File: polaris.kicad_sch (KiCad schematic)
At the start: 19 parts, among them J101 XT60-M, J102 PYRO0, J103 PYRO1, J104 PYRO2, J105 PYRO3, J106 PYRO4, J107 PYRO5, J108 FIN1, J109 FIN2, J110 FIN3, J111 FIN4

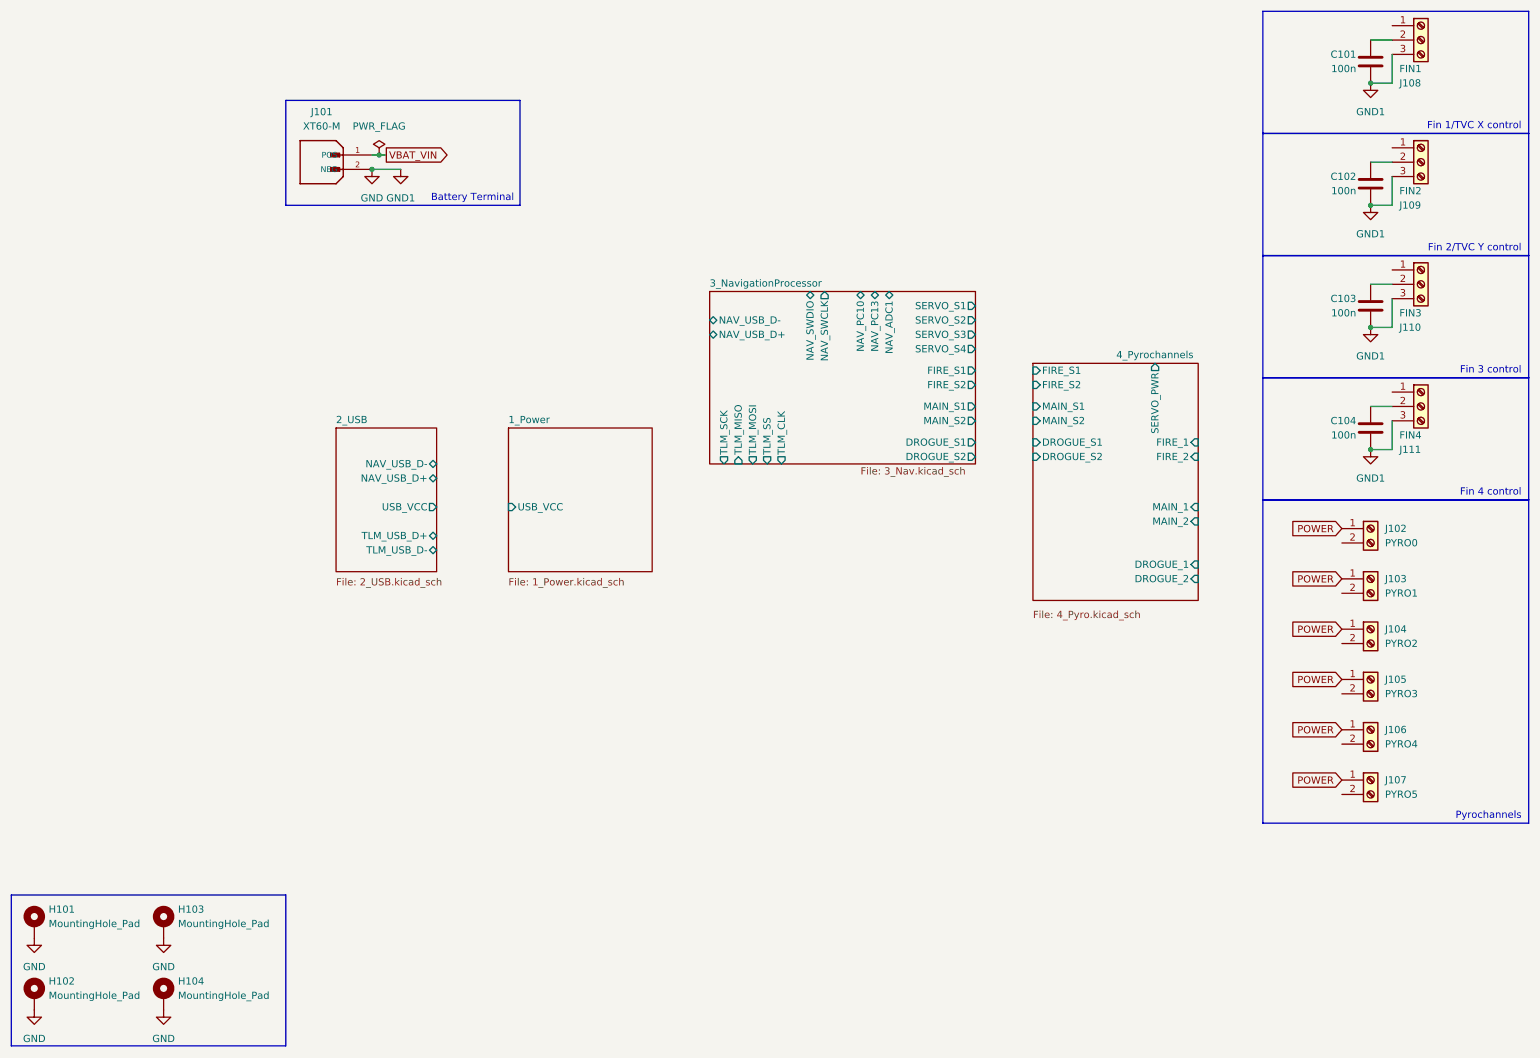
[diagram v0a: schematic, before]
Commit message: Finished restructuring schematic
Most components that were on page 3 are now in their own page
Added high-frequency 4.7 uF capacitor to servo power line
Continuity sensing on pyrochannels is multiplexed to one ADC on NAV.
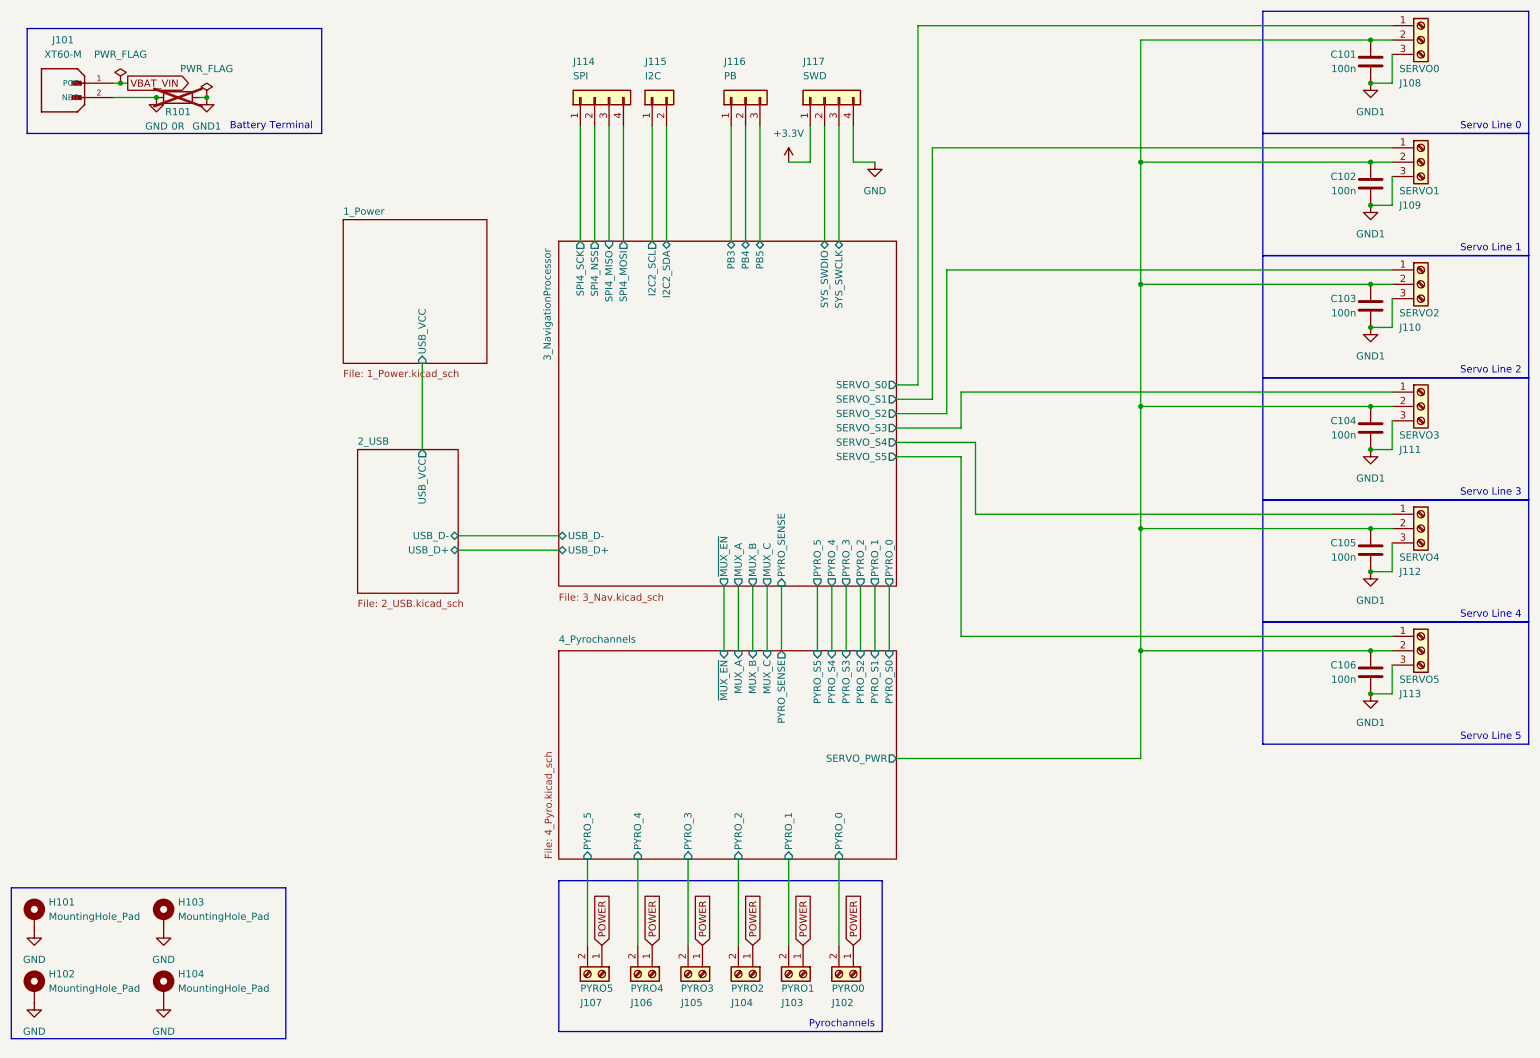
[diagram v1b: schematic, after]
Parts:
- added C105, C106: 100n, Capacitor_SMD:C_0603_1608Metric, symbol Device:C
- added J112: SERVO4, TerminalBlock:TerminalBlock_Xinya_XY308-2.54-3P_1x03_P2.54mm_Horizontal, symbol Connector:Screw_Terminal_01x03
- added J113: SERVO5, TerminalBlock:TerminalBlock_Xinya_XY308-2.54-3P_1x03_P2.54mm_Horizontal, symbol Connector:Screw_Terminal_01x03
- added J114: SPI, TerminalBlock:TerminalBlock_Xinya_XY308-2.54-4P_1x04_P2.54mm_Horizontal, symbol Connector_Generic:Conn_01x04
- added J115: I2C, TerminalBlock:TerminalBlock_Xinya_XY308-2.54-2P_1x02_P2.54mm_Horizontal, symbol Connector_Generic:Conn_01x02
- added J116: PB, TerminalBlock:TerminalBlock_Xinya_XY308-2.54-3P_1x03_P2.54mm_Horizontal, symbol Connector_Generic:Conn_01x03
- added J117: SWD, TerminalBlock:TerminalBlock_Xinya_XY308-2.54-4P_1x04_P2.54mm_Horizontal, symbol Connector_Generic:Conn_01x04
- added R101: 0R, Resistor_SMD:R_0603_1608Metric, symbol Device:R
- J108: value FIN1 -> SERVO0
- J109: value FIN2 -> SERVO1
- J110: value FIN3 -> SERVO2
- J111: value FIN4 -> SERVO3
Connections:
- net 3_NavigationProcessor/SERVO_S1: now also J109.1 (Pin_1)
- net 3_NavigationProcessor/SERVO_S2: now also J110.1 (Pin_1)
- net 3_NavigationProcessor/SERVO_S3: now also J111.1 (Pin_1)
- net 3_NavigationProcessor/SERVO_S4: now also J112.1 (Pin_1)
- net 4_Pyrochannels/SERVO_PWR: now also C101.1, C102.1, C103.1, C104.1, J108.2 (Pin_2), J109.2 (Pin_2), J110.2 (Pin_2), J111.2 (Pin_2), C105.1, C106.1, J112.2 (Pin_2), J113.2 (Pin_2)
- net GND: now also J117.4 (Pin_4), R101.1; no longer C101.2, C102.2, C103.2, C104.2, J108.3 (Pin_3), J109.3 (Pin_3), J110.3 (Pin_3), J111.3 (Pin_3)
- net 4_Pyrochannels/PYRO_5: now reaches J107.2 (Pin_2)
- net 3_NavigationProcessor/SERVO_S0: now reaches J108.1 (Pin_1)
- net 4_Pyrochannels/PYRO_1: now reaches J103.2 (Pin_2)
- net 4_Pyrochannels/PYRO_0: now reaches J102.2 (Pin_2)
- net 4_Pyrochannels/PYRO_4: now reaches J106.2 (Pin_2)
- net 4_Pyrochannels/PYRO_2: now reaches J104.2 (Pin_2)
- net 4_Pyrochannels/PYRO_3: now reaches J105.2 (Pin_2)
- new net +3.3V: J117.1 (Pin_1)
- new net 3_NavigationProcessor/I2C2_SCL: J115.1 (Pin_1)
- new net 3_NavigationProcessor/I2C2_SDA: J115.2 (Pin_2)
- new net 3_NavigationProcessor/PB3: J116.1 (Pin_1)
- new net 3_NavigationProcessor/PB4: J116.2 (Pin_2)
- new net 3_NavigationProcessor/PB5: J116.3 (Pin_3)
- new net 3_NavigationProcessor/SERVO_S5: J113.1 (Pin_1)
- new net 3_NavigationProcessor/SPI4_MISO: J114.3 (Pin_3)
- new net 3_NavigationProcessor/SPI4_MOSI: J114.4 (Pin_4)
- new net 3_NavigationProcessor/SPI4_NSS: J114.2 (Pin_2)
- new net 3_NavigationProcessor/SPI4_SCK: J114.1 (Pin_1)
- new net 3_NavigationProcessor/SYS_SWCLK: J117.3 (Pin_3)
- new net 3_NavigationProcessor/SYS_SWDIO: J117.2 (Pin_2)
- new net GND1: C101.2, C102.2, C103.2, C104.2, C105.2, C106.2, J108.3 (Pin_3), J109.3 (Pin_3), J110.3 (Pin_3), J111.3 (Pin_3), J112.3 (Pin_3), J113.3 (Pin_3), R101.2
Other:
- sheet 2_USB ports: added USB_D+, USB_D-; removed NAV_USB_D+, NAV_USB_D-, TLM_USB_D+, TLM_USB_D-
- sheet 3_NavigationProcessor ports: added I2C2_SCL, I2C2_SDA, MUX_A, MUX_B, MUX_C, PB3, PB4, PB5, PYRO_0, PYRO_1, PYRO_2, PYRO_3, PYRO_4, PYRO_5, PYRO_SENSE, SERVO_S0, SERVO_S5, SPI4_MISO, SPI4_MOSI, SPI4_NSS, SPI4_SCK, SYS_SWCLK, SYS_SWDIO, USB_D+, USB_D-, ~{MUX_EN}; removed DROGUE_S1, DROGUE_S2, FIRE_S1, FIRE_S2, MAIN_S1, MAIN_S2, NAV_ADC1, NAV_PC10, NAV_PC13, NAV_SWCLK, NAV_SWDIO, NAV_USB_D+, NAV_USB_D-, TLM_CLK, TLM_MISO, TLM_MOSI, TLM_SCK, TLM_SS
- sheet 4_Pyrochannels ports: added MUX_A, MUX_B, MUX_C, PYRO_0, PYRO_1, PYRO_2, PYRO_3, PYRO_4, PYRO_5, PYRO_S0, PYRO_S1, PYRO_S2, PYRO_S3, PYRO_S4, PYRO_S5, PYRO_SENSE, ~{MUX_EN}; removed DROGUE_1, DROGUE_2, DROGUE_S1, DROGUE_S2, FIRE_1, FIRE_2, FIRE_S1, FIRE_S2, MAIN_1, MAIN_2, MAIN_S1, MAIN_S2
- note added: "Servo Line 0"
- note added: "Servo Line 1"
- note added: "Servo Line 2"
- note added: "Servo Line 3"
- note added: "Servo Line 4"
- note added: "Servo Line 5"
- note removed: "Fin 1/TVC X control"
- note removed: "Fin 2/TVC Y control"
- note removed: "Fin 3 control"
- note removed: "Fin 4 control"
- moved on the sheet: H101, H102, H103, H104, J101, J102, J103, J104, J105, J106, J107

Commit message: Updated schematic so that servo GND and signal GND are no longer separate
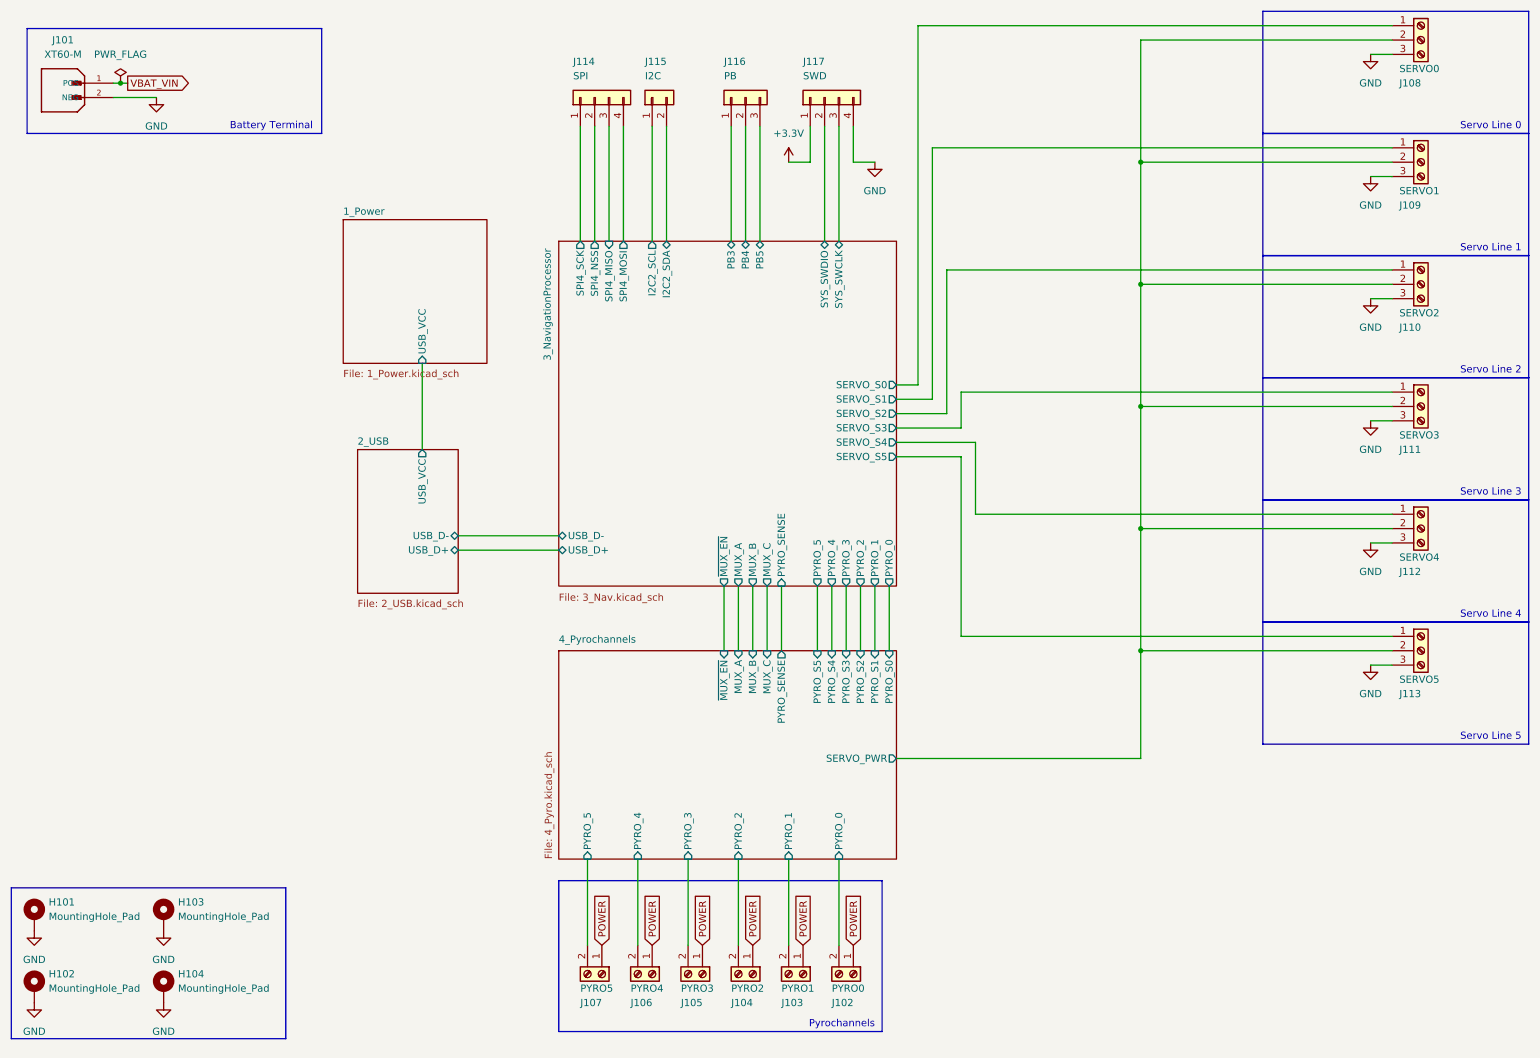
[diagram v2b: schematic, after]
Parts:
- removed C101, C102, C103, C104, C105, C106: 100n, Capacitor_SMD:C_0603_1608Metric, symbol Device:C
- removed R101: 0R, Resistor_SMD:R_0603_1608Metric, symbol Device:R
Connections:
- net GND1 is gone; now on net GND: J108.3 (Pin_3), J109.3 (Pin_3), J110.3 (Pin_3), J111.3 (Pin_3), J112.3 (Pin_3), J113.3 (Pin_3)

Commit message: Re-annotated schematic
Continued laying out traces on PCB
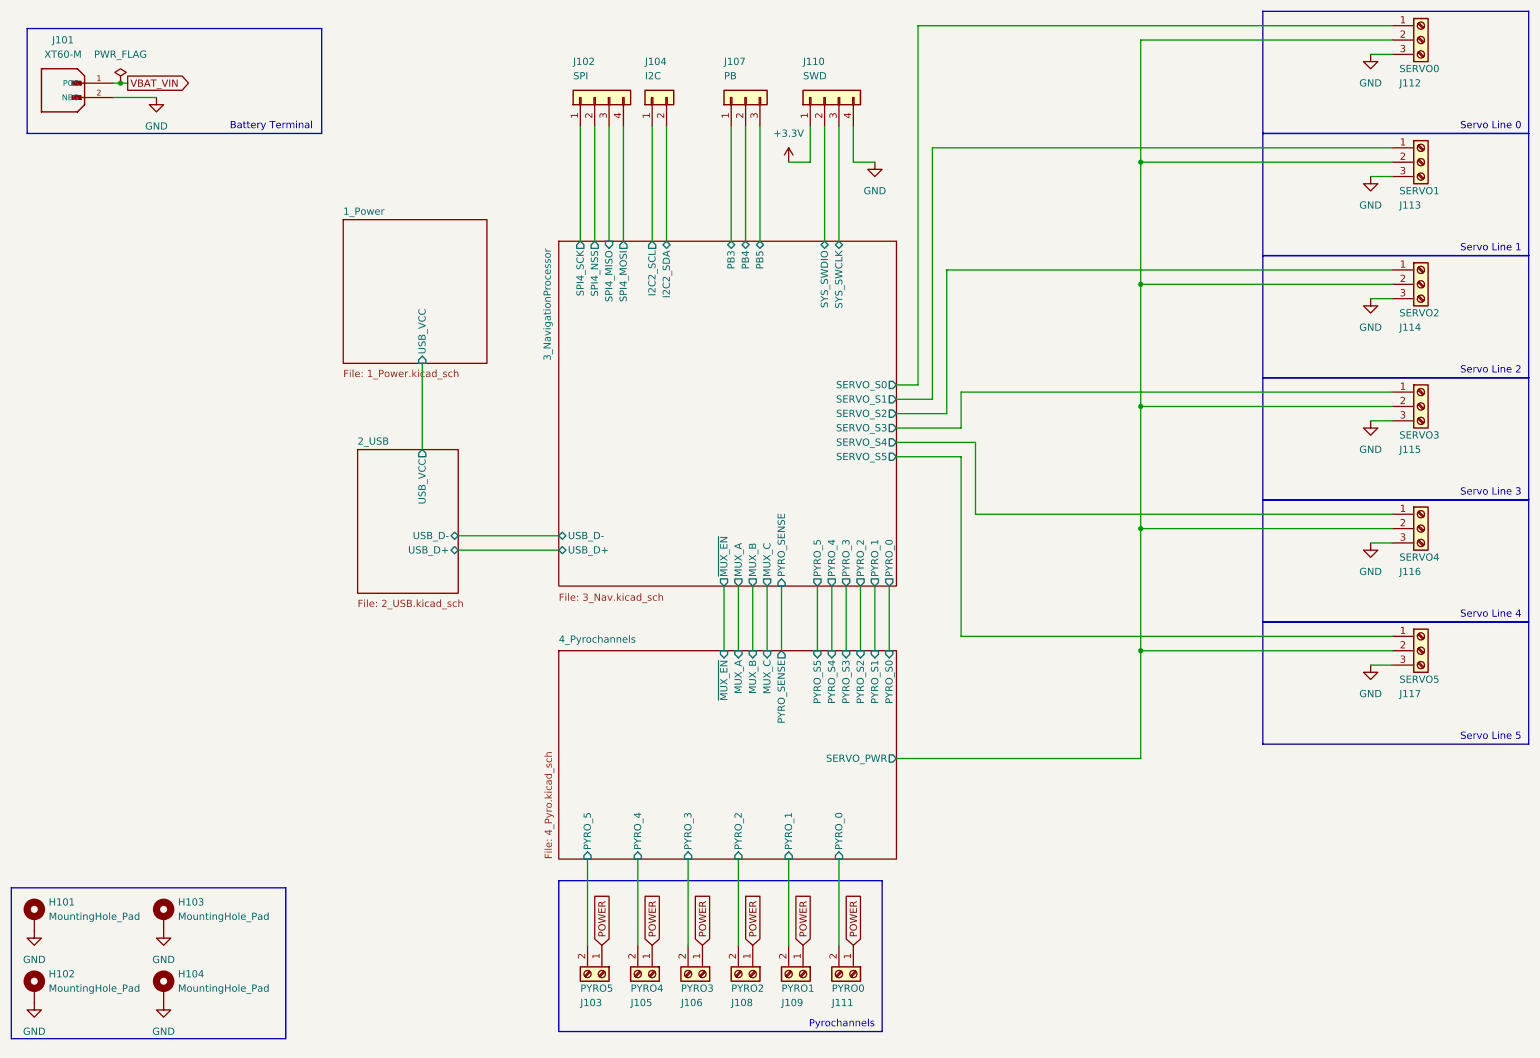
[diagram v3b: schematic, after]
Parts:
- removed J105: PYRO3, TerminalBlock:TerminalBlock_Xinya_XY308-2.54-2P_1x02_P2.54mm_Horizontal, symbol Connector:Screw_Terminal_01x02
- added J106: PYRO3, TerminalBlock:TerminalBlock_Xinya_XY308-2.54-2P_1x02_P2.54mm_Horizontal, symbol Connector:Screw_Terminal_01x02
- renumbered J114 to J102, J107 to J103, J115 to J104, J106 to J105, J116 to J107, J104 to J108, J103 to J109, J117 to J110, J102 to J111, J108 to J112, J109 to J113, J110 to J114, J111 to J115, J112 to J116, J113 to J117
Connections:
- net 4_Pyrochannels/PYRO_3: now also J106.2 (Pin_2)
- net POWER: now also J106.1 (Pin_1)
